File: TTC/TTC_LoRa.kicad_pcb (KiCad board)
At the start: 2 copper layers, 84.2 x 84.2 mm, 81 parts, among them J1 EPS 3V3, J2 MISSION, J3 SMA edge, J4 SWD TC2030, J5 OBC I2C, J6 OBC UART, J7 EPS 5V, J8 SPARE GPIO, J9 DIPOLE FEED, Q1 AO3401A, U1 TPS7A2033PDBVR, U2 RFM98W-433S2, U3 STM32F446RET6, U4 TMP102, Y1 8MHz, Y2 32.768kHz

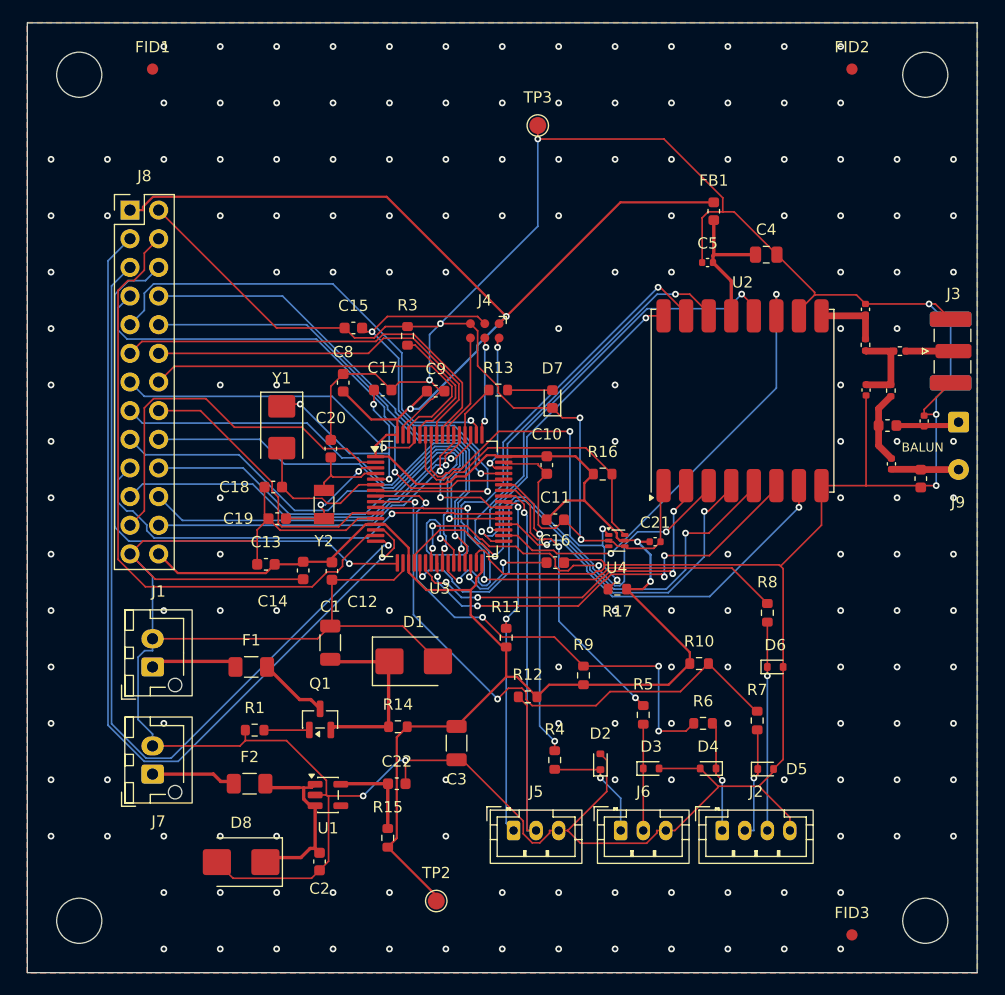
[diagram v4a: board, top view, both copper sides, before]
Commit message: TTC: resize board to 85 x 84 mm and move mounting holes per measured drawing
Outline 85 x 84 mm (was 84.2 x 84.2). Holes now 74 x 76 mm pitch,
5.5 mm from left/right edges and 4 mm from top/bottom (was 75 x 75).
GND pours reshaped to the new outline and refilled. DRC: 0 violations,
0 unconnected. README updated to match.

Co-Authored-By: Claude Sonnet 5.5 <noreply@anthropic.com>
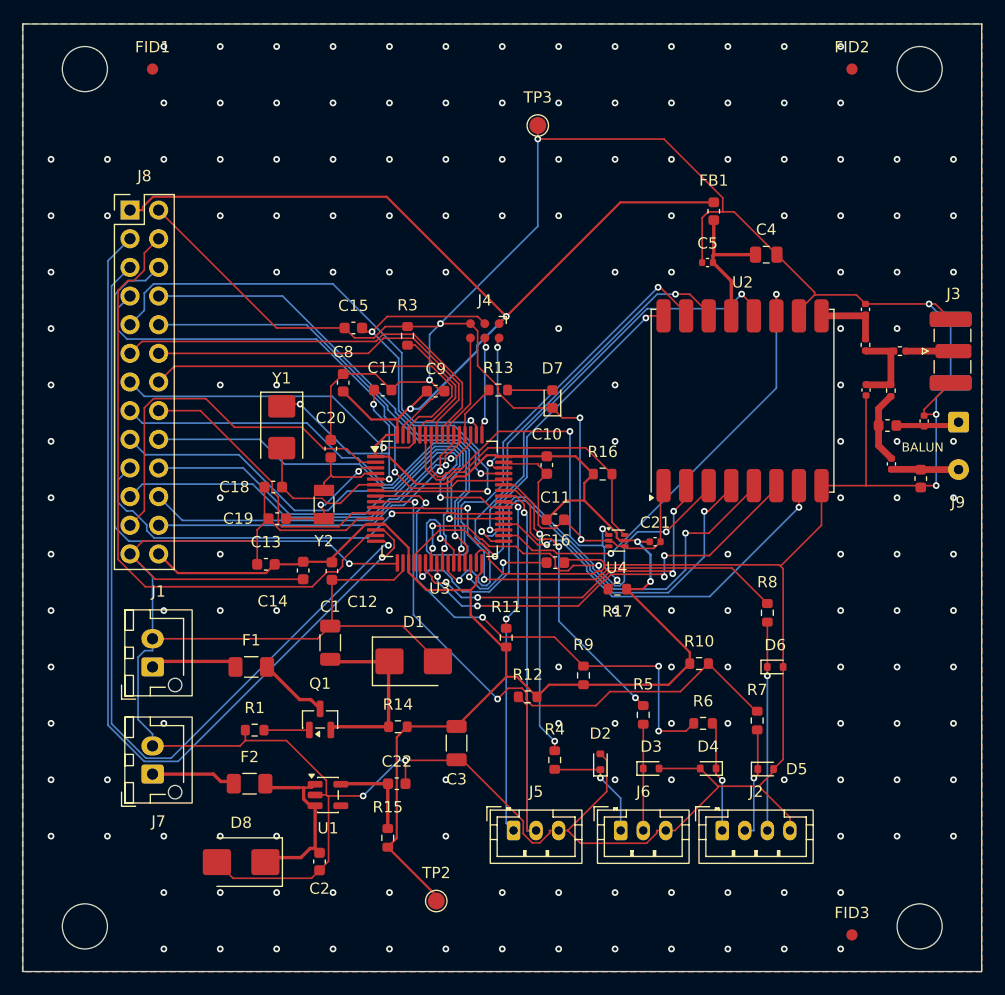
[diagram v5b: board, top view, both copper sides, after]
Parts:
- moved H1 0.71 mm to (98.0, 97.0)
- moved H2 0.71 mm to (172.0, 97.0)
- moved H3 0.71 mm to (98.0, 173.0)
- moved H4 0.71 mm to (172.0, 173.0)
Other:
- board size 84.2 x 84.2 mm -> 85 x 84 mm
